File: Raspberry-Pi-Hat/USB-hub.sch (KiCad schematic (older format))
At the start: 4 parts

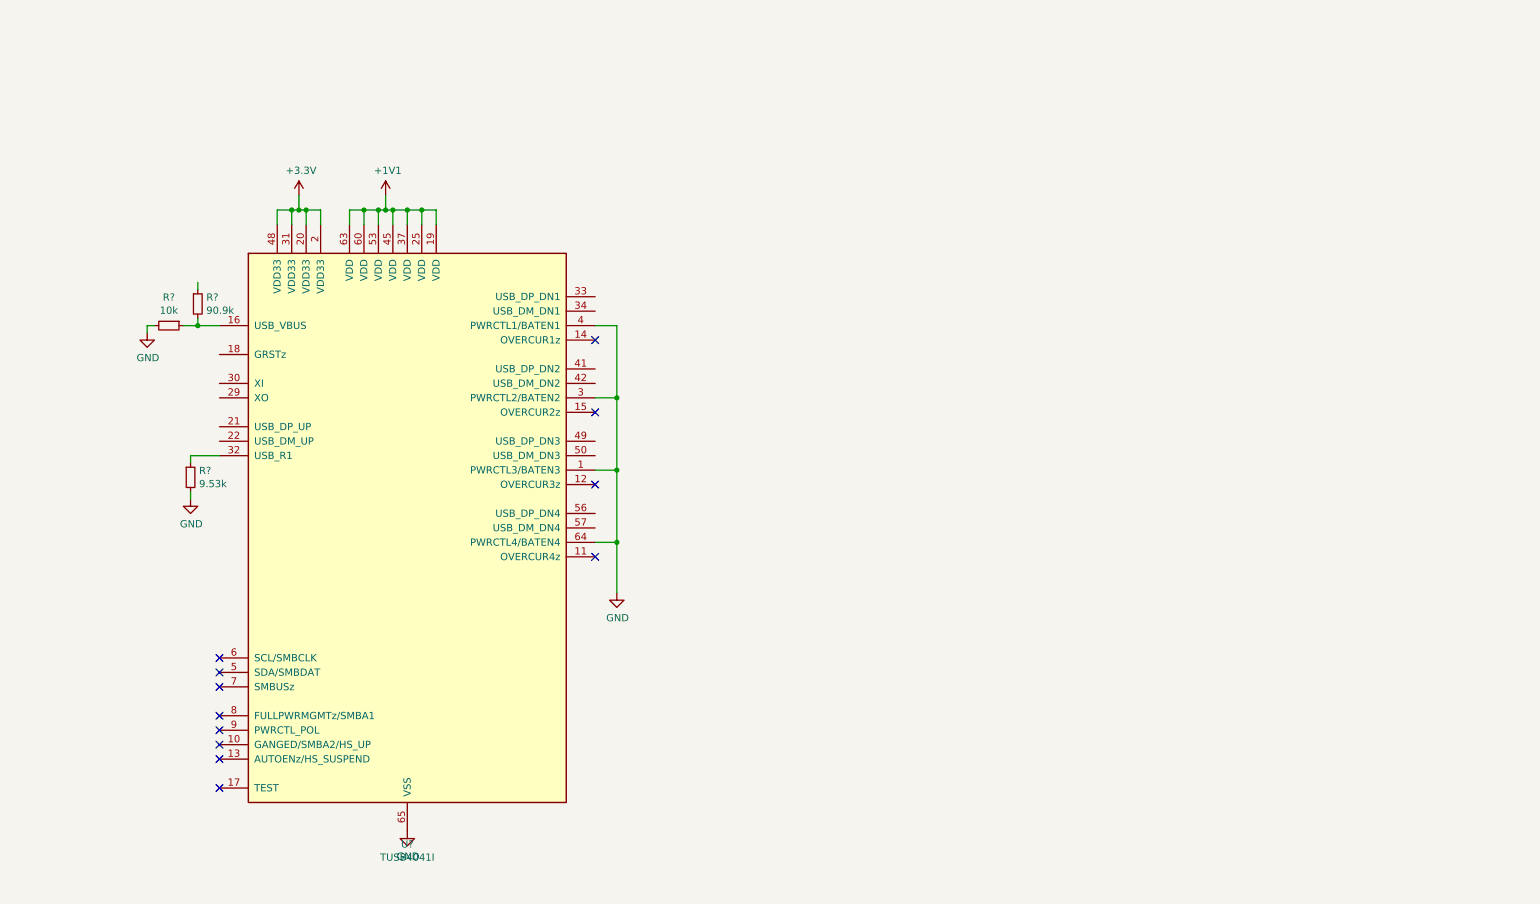
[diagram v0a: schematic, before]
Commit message: USB-HUB
Implementation of USB HUB
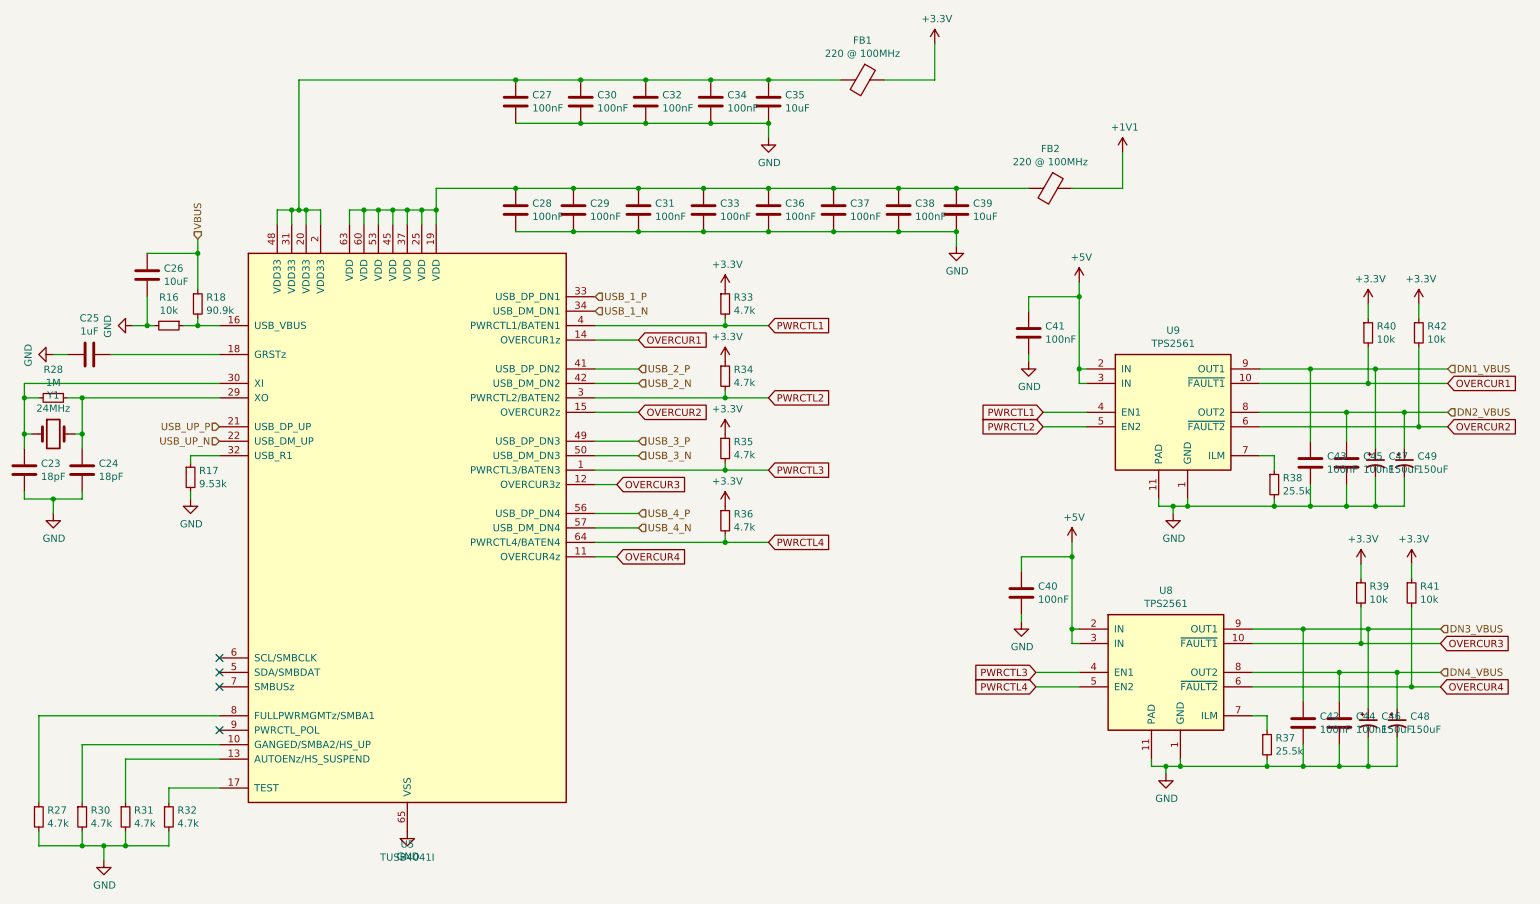
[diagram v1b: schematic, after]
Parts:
- added C23, C24: 18pF, symbol Device:C
- added C25: 1uF, symbol Device:C
- added C26, C35, C39: 10uF, symbol Device:C
- added C27, C28, C29, C30, C31, C32, C33, C34, C36, C37, C38, C40, C41, C42, C43, C44, C45: 100nF, symbol Device:C
- added C46, C47, C48, C49: 150uF, symbol Device:CP1_Small
- added FB1, FB2: 220 @ 100MHz, symbol Device:Ferrite_Bead
- added R27, R30, R31, R32, R33, R34, R35, R36: 4.7k, symbol Device:R_Small
- added R28: 1M, symbol Device:R_Small
- added R37, R38: 25.5k, symbol Device:R_Small
- added R39, R40, R41, R42: 10k, symbol Device:R_Small
- added U8, U9: TPS2561, Package_SON:VSON-10-1EP_3x3mm_P0.5mm_EP1.65x2.4mm_ThermalVias, symbol Interface_USB:TPS2561
- added Y1: 24MHz, symbol Device:Crystal
- gave numbers to parts that had none: 4
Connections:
- net labels added: +5V, DN1_VBUS, DN2_VBUS, DN3_VBUS, DN4_VBUS, OVERCUR1, OVERCUR2, OVERCUR3, OVERCUR4, PWRCTL1, PWRCTL2, PWRCTL3, PWRCTL4, USB_1_N, USB_1_P, USB_2_N, USB_2_P, USB_3_N, USB_3_P, USB_4_N, USB_4_P, USB_UP_N, USB_UP_P, VBUS
- wire segments 41 -> 214
- no-connect marks 12 -> 4

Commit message: Starting placing component
Assigned component footprint and started placing component on the board
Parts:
- C23, C24, C25, C26, C27, C28, C29, C30, C31, C32, C33, C34, C35, C36, C37, C38, C39, C40, C41, C42, C43, C44, C45, C46, C47, C48, C49: footprint (none) -> Capacitor_SMD:C_1206_3216Metric_Pad1.42x1.75mm_HandSolder
- FB1, FB2: footprint (none) -> Resistor_SMD:R_0805_2012Metric_Pad1.15x1.40mm_HandSolder
- R16, R17, R18, R27, R28, R30, R31, R32, R33, R34, R35, R36, R37, R38, R39, R40, R41, R42: footprint (none) -> Resistor_SMD:R_0603_1608Metric_Pad1.05x0.95mm_HandSolder
- Y1: footprint (none) -> Crystal:Crystal_SMD_Abracon_ABM3-2Pin_5.0x3.2mm_HandSoldering

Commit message: changed footprint size
changed resistor and capacitor footprint size for 0603 when possible.
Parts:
- C23, C24, C25, C26, C27, C28, C29, C30, C31, C32, C33, C34, C35, C36, C37, C38, C39, C40, C41, C42, C43, C44, C45: footprint Capacitor_SMD:C_1206_3216Metric_Pad1.42x1.75mm_HandSolder -> Capacitor_SMD:C_0603_1608Metric_Pad1.05x0.95mm_HandSolder
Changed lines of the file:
@@
 F 0 "C26" H 6135 3404 50  0000 R CNN
 F 1 "10uF" H 6135 3495 50  0000 R CNN
-F 2 "Capacitor_SMD:C_1206_3216Metric_Pad1.42x1.75mm_HandSolder" H 6288 3300 50  0001 C CNN
+F 2 "Capacitor_SMD:C_0603_1608Metric_Pad1.05x0.95mm_HandSolder" H 6288 3300 50  0001 C CNN
 F 3 "~" H 6250 3450 50  0001 C CNN
 	1    6250 3450
@@
 F 0 "C23" H 5285 4754 50  0000 R CNN
 F 1 "18pF" H 5285 4845 50  0000 R CNN
-F 2 "Capacitor_SMD:C_1206_3216Metric_Pad1.42x1.75mm_HandSolder" H 5438 4650 50  0001 C CNN
+F 2 "Capacitor_SMD:C_0603_1608Metric_Pad1.05x0.95mm_HandSolder" H 5438 4650 50  0001 C CNN
 F 3 "~" H 5400 4800 50  0001 C CNN
 	1    5400 4800
@@
 F 0 "C24" H 5685 4754 50  0000 R CNN
 F 1 "18pF" H 5685 4845 50  0000 R CNN
-F 2 "Capacitor_SMD:C_1206_3216Metric_Pad1.42x1.75mm_HandSolder" H 5838 4650 50  0001 C CNN
+F 2 "Capacitor_SMD:C_0603_1608Metric_Pad1.05x0.95mm_HandSolder" H 5838 4650 50  0001 C CNN
 F 3 "~" H 5800 4800 50  0001 C CNN
 	1    5800 4800
@@
 F 0 "C25" V 6102 4000 50  0000 C CNN
 F 1 "1uF" V 6011 4000 50  0000 C CNN
-F 2 "Capacitor_SMD:C_1206_3216Metric_Pad1.42x1.75mm_HandSolder" H 5888 3850 50  0001 C CNN
+F 2 "Capacitor_SMD:C_0603_1608Metric_Pad1.05x0.95mm_HandSolder" H 5888 3850 50  0001 C CNN
 F 3 "~" H 5850 4000 50  0001 C CNN
 	1    5850 4000
@@
 F 0 "C39" H 11965 3046 50  0000 L CNN
 F 1 "10uF" H 11965 2955 50  0000 L CNN
-F 2 "Capacitor_SMD:C_1206_3216Metric_Pad1.42x1.75mm_HandSolder" H 11888 2850 50  0001 C CNN
+F 2 "Capacitor_SMD:C_0603_1608Metric_Pad1.05x0.95mm_HandSolder" H 11888 2850 50  0001 C CNN
 F 3 "~" H 11850 3000 50  0001 C CNN
 	1    11850 3000
@@
 F 0 "C38" H 11565 3046 50  0000 L CNN
 F 1 "100nF" H 11565 2955 50  0000 L CNN
-F 2 "Capacitor_SMD:C_1206_3216Metric_Pad1.42x1.75mm_HandSolder" H 11488 2850 50  0001 C CNN
+F 2 "Capacitor_SMD:C_0603_1608Metric_Pad1.05x0.95mm_HandSolder" H 11488 2850 50  0001 C CNN
 F 3 "~" H 11450 3000 50  0001 C CNN
 	1    11450 3000
@@
 F 0 "C37" H 11115 3046 50  0000 L CNN
 F 1 "100nF" H 11115 2955 50  0000 L CNN
-F 2 "Capacitor_SMD:C_1206_3216Metric_Pad1.42x1.75mm_HandSolder" H 11038 2850 50  0001 C CNN
+F 2 "Capacitor_SMD:C_0603_1608Metric_Pad1.05x0.95mm_HandSolder" H 11038 2850 50  0001 C CNN
 F 3 "~" H 11000 3000 50  0001 C CNN
 	1    11000 3000
@@
 F 0 "C36" H 10665 3046 50  0000 L CNN
 F 1 "100nF" H 10665 2955 50  0000 L CNN
-F 2 "Capacitor_SMD:C_1206_3216Metric_Pad1.42x1.75mm_HandSolder" H 10588 2850 50  0001 C CNN
+F 2 "Capacitor_SMD:C_0603_1608Metric_Pad1.05x0.95mm_HandSolder" H 10588 2850 50  0001 C CNN
 F 3 "~" H 10550 3000 50  0001 C CNN
 	1    10550 3000
@@
 F 0 "C33" H 10215 3046 50  0000 L CNN
 F 1 "100nF" H 10215 2955 50  0000 L CNN
-F 2 "Capacitor_SMD:C_1206_3216Metric_Pad1.42x1.75mm_HandSolder" H 10138 2850 50  0001 C CNN
+F 2 "Capacitor_SMD:C_0603_1608Metric_Pad1.05x0.95mm_HandSolder" H 10138 2850 50  0001 C CNN
 F 3 "~" H 10100 3000 50  0001 C CNN
 	1    10100 3000
@@
 F 0 "C31" H 9765 3046 50  0000 L CNN
 F 1 "100nF" H 9765 2955 50  0000 L CNN
-F 2 "Capacitor_SMD:C_1206_3216Metric_Pad1.42x1.75mm_HandSolder" H 9688 2850 50  0001 C CNN
+F 2 "Capacitor_SMD:C_0603_1608Metric_Pad1.05x0.95mm_HandSolder" H 9688 2850 50  0001 C CNN
 F 3 "~" H 9650 3000 50  0001 C CNN
 	1    9650 3000
@@
 F 0 "C29" H 9315 3046 50  0000 L CNN
 F 1 "100nF" H 9315 2955 50  0000 L CNN
-F 2 "Capacitor_SMD:C_1206_3216Metric_Pad1.42x1.75mm_HandSolder" H 9238 2850 50  0001 C CNN
+F 2 "Capacitor_SMD:C_0603_1608Metric_Pad1.05x0.95mm_HandSolder" H 9238 2850 50  0001 C CNN
 F 3 "~" H 9200 3000 50  0001 C CNN
 	1    9200 3000
@@
 F 0 "C28" H 8915 3046 50  0000 L CNN
 F 1 "100nF" H 8915 2955 50  0000 L CNN
-F 2 "Capacitor_SMD:C_1206_3216Metric_Pad1.42x1.75mm_HandSolder" H 8838 2850 50  0001 C CNN
+F 2 "Capacitor_SMD:C_0603_1608Metric_Pad1.05x0.95mm_HandSolder" H 8838 2850 50  0001 C CNN
 F 3 "~" H 8800 3000 50  0001 C CNN
 	1    8800 3000
@@
 F 0 "C35" H 10665 2296 50  0000 L CNN
 F 1 "10uF" H 10665 2205 50  0000 L CNN
-F 2 "Capacitor_SMD:C_1206_3216Metric_Pad1.42x1.75mm_HandSolder" H 10588 2100 50  0001 C CNN
+F 2 "Capacitor_SMD:C_0603_1608Metric_Pad1.05x0.95mm_HandSolder" H 10588 2100 50  0001 C CNN
 F 3 "~" H 10550 2250 50  0001 C CNN
 	1    10550 2250
@@
 F 0 "C34" H 10265 2296 50  0000 L CNN
 F 1 "100nF" H 10265 2205 50  0000 L CNN
-F 2 "Capacitor_SMD:C_1206_3216Metric_Pad1.42x1.75mm_HandSolder" H 10188 2100 50  0001 C CNN
+F 2 "Capacitor_SMD:C_0603_1608Metric_Pad1.05x0.95mm_HandSolder" H 10188 2100 50  0001 C CNN
 F 3 "~" H 10150 2250 50  0001 C CNN
 	1    10150 2250
@@
 F 0 "C32" H 9815 2296 50  0000 L CNN
 F 1 "100nF" H 9815 2205 50  0000 L CNN
-F 2 "Capacitor_SMD:C_1206_3216Metric_Pad1.42x1.75mm_HandSolder" H 9738 2100 50  0001 C CNN
+F 2 "Capacitor_SMD:C_0603_1608Metric_Pad1.05x0.95mm_HandSolder" H 9738 2100 50  0001 C CNN
 F 3 "~" H 9700 2250 50  0001 C CNN
 	1    9700 2250
@@
 F 0 "C30" H 9365 2296 50  0000 L CNN
 F 1 "100nF" H 9365 2205 50  0000 L CNN
-F 2 "Capacitor_SMD:C_1206_3216Metric_Pad1.42x1.75mm_HandSolder" H 9288 2100 50  0001 C CNN
+F 2 "Capacitor_SMD:C_0603_1608Metric_Pad1.05x0.95mm_HandSolder" H 9288 2100 50  0001 C CNN
 F 3 "~" H 9250 2250 50  0001 C CNN
 	1    9250 2250
@@
 F 0 "C27" H 8915 2296 50  0000 L CNN
 F 1 "100nF" H 8915 2205 50  0000 L CNN
-F 2 "Capacitor_SMD:C_1206_3216Metric_Pad1.42x1.75mm_HandSolder" H 8838 2100 50  0001 C CNN
+F 2 "Capacitor_SMD:C_0603_1608Metric_Pad1.05x0.95mm_HandSolder" H 8838 2100 50  0001 C CNN
 F 3 "~" H 8800 2250 50  0001 C CNN
 	1    8800 2250
@@
 F 0 "C40" H 12415 5696 50  0000 L CNN
 F 1 "100nF" H 12415 5605 50  0000 L CNN
-F 2 "Capacitor_SMD:C_1206_3216Metric_Pad1.42x1.75mm_HandSolder" H 12338 5500 50  0001 C CNN
+F 2 "Capacitor_SMD:C_0603_1608Metric_Pad1.05x0.95mm_HandSolder" H 12338 5500 50  0001 C CNN
 F 3 "~" H 12300 5650 50  0001 C CNN
 	1    12300 5650
@@
 F 0 "C42" H 14365 6596 50  0000 L CNN
 F 1 "100nF" H 14365 6505 50  0000 L CNN
-F 2 "Capacitor_SMD:C_1206_3216Metric_Pad1.42x1.75mm_HandSolder" H 14288 6400 50  0001 C CNN
+F 2 "Capacitor_SMD:C_0603_1608Metric_Pad1.05x0.95mm_HandSolder" H 14288 6400 50  0001 C CNN
 F 3 "~" H 14250 6550 50  0001 C CNN
 	1    14250 6550
@@
 F 0 "C44" H 14615 6596 50  0000 L CNN
 F 1 "100nF" H 14615 6505 50  0000 L CNN
-F 2 "Capacitor_SMD:C_1206_3216Metric_Pad1.42x1.75mm_HandSolder" H 14538 6400 50  0001 C CNN
+F 2 "Capacitor_SMD:C_0603_1608Metric_Pad1.05x0.95mm_HandSolder" H 14538 6400 50  0001 C CNN
 F 3 "~" H 14500 6550 50  0001 C CNN
 	1    14500 6550
@@
 F 0 "C41" H 12465 3896 50  0000 L CNN
 F 1 "100nF" H 12465 3805 50  0000 L CNN
-F 2 "Capacitor_SMD:C_1206_3216Metric_Pad1.42x1.75mm_HandSolder" H 12388 3700 50  0001 C CNN
+F 2 "Capacitor_SMD:C_0603_1608Metric_Pad1.05x0.95mm_HandSolder" H 12388 3700 50  0001 C CNN
 F 3 "~" H 12350 3850 50  0001 C CNN
 	1    12350 3850
@@
 F 0 "C43" H 14415 4796 50  0000 L CNN
 F 1 "100nF" H 14415 4705 50  0000 L CNN
-F 2 "Capacitor_SMD:C_1206_3216Metric_Pad1.42x1.75mm_HandSolder" H 14338 4600 50  0001 C CNN
+F 2 "Capacitor_SMD:C_0603_1608Metric_Pad1.05x0.95mm_HandSolder" H 14338 4600 50  0001 C CNN
 F 3 "~" H 14300 4750 50  0001 C CNN
 	1    14300 4750
@@
 F 0 "C45" H 14665 4796 50  0000 L CNN
 F 1 "100nF" H 14665 4705 50  0000 L CNN
-F 2 "Capacitor_SMD:C_1206_3216Metric_Pad1.42x1.75mm_HandSolder" H 14588 4600 50  0001 C CNN
+F 2 "Capacitor_SMD:C_0603_1608Metric_Pad1.05x0.95mm_HandSolder" H 14588 4600 50  0001 C CNN
 F 3 "~" H 14550 4750 50  0001 C CNN
 	1    14550 4750

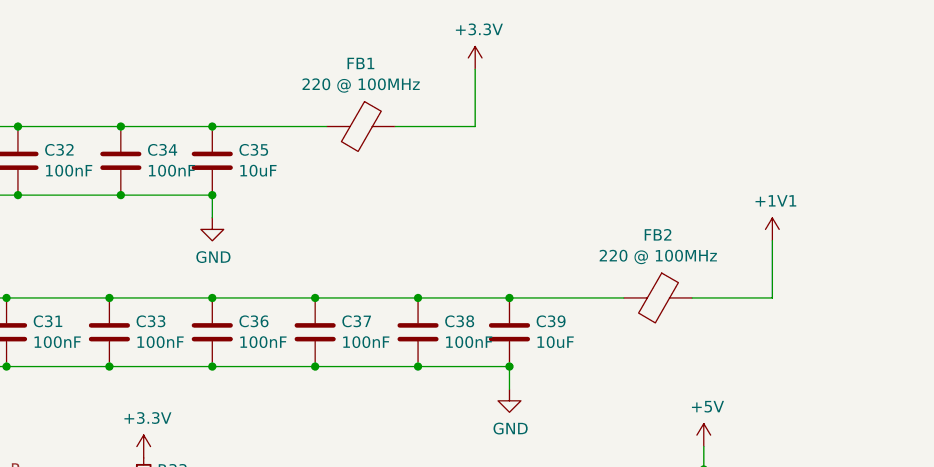
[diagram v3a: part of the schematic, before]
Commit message: Routted diff pair
All USB lines is routed and most of the signal lines is routed as well.
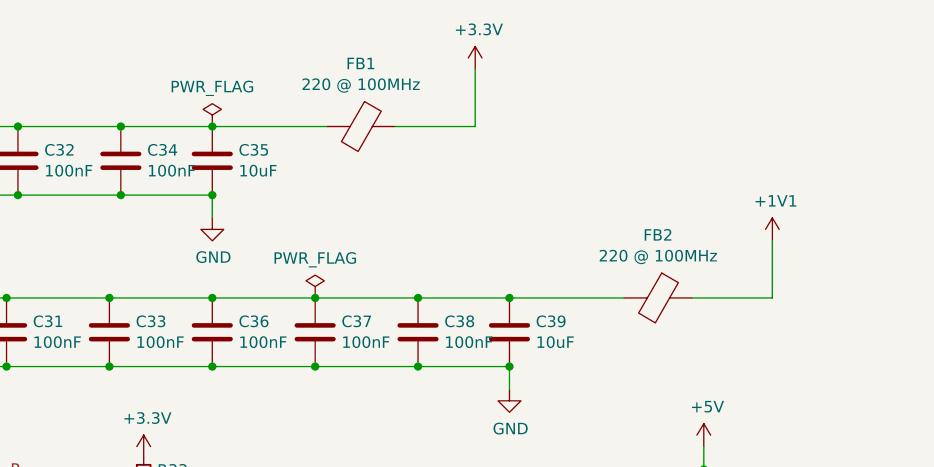
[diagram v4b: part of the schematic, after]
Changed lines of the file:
@@
 	12650 2850 13000 2850
-Wire Wire Line
-	13000 2850 13000 2600
 Wire Wire Line
 	7850 3000 7950 3000
@@
 Wire Wire Line
 	11350 2100 11700 2100
-Wire Wire Line
-	11700 2100 11700 1850
 Wire Wire Line
 	7300 2100 7300 3000
@@
 	1    0    0    -1
 $EndComp
+Wire Wire Line
+	11700 1850 11700 2100
+Wire Wire Line
+	13000 2600 13000 2850
+$Comp
+L power:PWR_FLAG #FLG0105
+U 1 1 5F1CCEC6
+P 10550 2100
+F 0 "#FLG0105" H 10550 2175 50  0001 C CNN
+F 1 "PWR_FLAG" H 10550 2273 50  0000 C CNN
+F 2 "" H 10550 2100 50  0001 C CNN
+F 3 "~" H 10550 2100 50  0001 C CNN
+	1    10550 2100
+	1    0    0    -1
+$EndComp
+$Comp
+L power:PWR_FLAG #FLG0106
+U 1 1 5F1CD35C
+P 11000 2850
+F 0 "#FLG0106" H 11000 2925 50  0001 C CNN
+F 1 "PWR_FLAG" H 11000 3023 50  0000 C CNN
+F 2 "" H 11000 2850 50  0001 C CNN
+F 3 "~" H 11000 2850 50  0001 C CNN
+	1    11000 2850
+	1    0    0    -1
+$EndComp
